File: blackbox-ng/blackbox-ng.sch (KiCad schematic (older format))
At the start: 5 parts

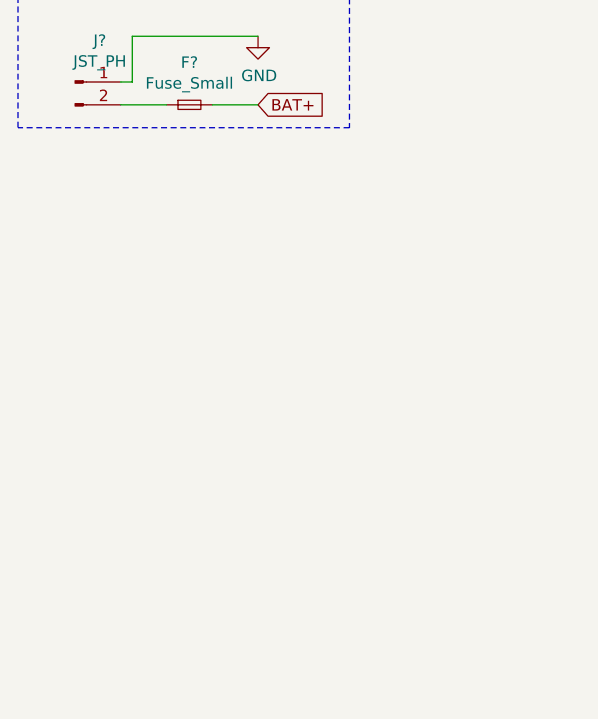
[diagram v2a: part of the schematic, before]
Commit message: add power led
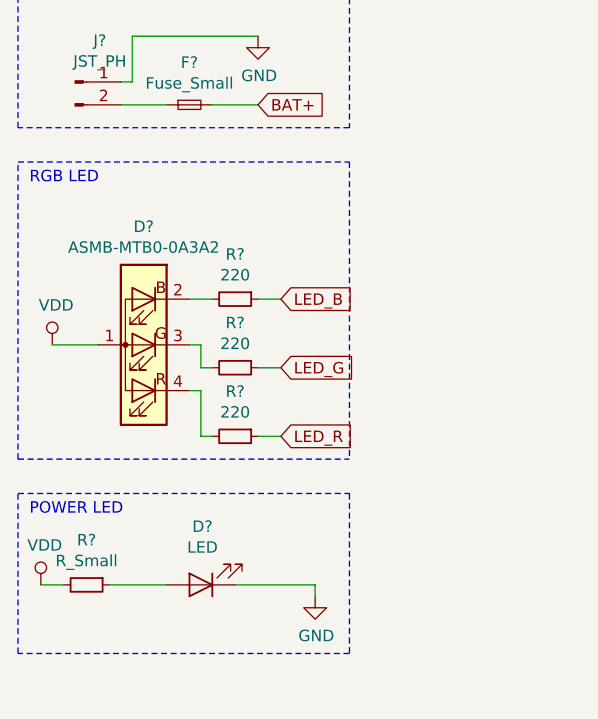
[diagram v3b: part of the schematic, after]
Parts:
- added D?: ASMB-MTB0-0A3A2, LED_SMD:LED_Avago_PLCC4_3.2x2.8mm_CW, symbol LED:ASMB-MTB0-0A3A2
- added D?: LED, symbol Device:LED
- added R? (x3): 220, symbol Device:R_Small
- added R?: R_Small, symbol Device:R_Small
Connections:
- net GND: now also D?.1 (K)
- net VDD: now also D?.1 (A), R?.2
- new net: D?.2 (BK), R?.2
- new net: D?.3 (GK), R?.2
- new net: D?.4 (RK), R?.2
- new net: D?.2 (A), R?.1
- new net LED_B: R?.1
- new net LED_G: R?.1
- new net LED_R: R?.1
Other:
- note added: "POWER LED"
- note added: "RGB LED"
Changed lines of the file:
@@
 Text Notes 650  1950 0    50   ~ 0
 BATTERY WITH FUSE
+$Comp
+L LED:ASMB-MTB0-0A3A2 D?
+U 1 1 5DF1D30C
+P 1150 3450
+F 0 "D?" H 1150 2933 50  0000 C CNN
+F 1 "ASMB-MTB0-0A3A2" H 1150 3024 50  0000 C CNN
+F 2 "LED_SMD:LED_Avago_PLCC4_3.2x2.8mm_CW" H 1150 3950 50  0001 C CNN
+F 3 "https://docs.broadcom.com/docs/AV02-4186EN" H 1150 3000 50  0001 C CNN
+	1    1150 3450
+	-1   0    0    1
+$EndComp
+$Comp
+L power:VDD #PWR?
+U 1 1 5DF22278
+P 750 3450
+F 0 "#PWR?" H 750 3300 50  0001 C CNN
+F 1 "VDD" H 767 3623 50  0000 C CNN
+F 2 "" H 750 3450 50  0001 C CNN
+F 3 "" H 750 3450 50  0001 C CNN
+	1    750  3450
+	1    0    0    -1
+$EndComp
+Wire Wire Line
+	750  3450 950  3450
+$Comp
+L Device:R_Small R?
+U 1 1 5DF22954
+P 1550 3250
+F 0 "R?" V 1354 3250 50  0000 C CNN
+F 1 "220" V 1445 3250 50  0000 C CNN
+F 2 "" H 1550 3250 50  0001 C CNN
+F 3 "~" H 1550 3250 50  0001 C CNN
+	1    1550 3250
+	0    1    1    0
+$EndComp
+$Comp
+L Device:R_Small R?
+U 1 1 5DF22E47
+P 1550 3550
+F 0 "R?" V 1354 3550 50  0000 C CNN
+F 1 "220" V 1445 3550 50  0000 C CNN
+F 2 "" H 1550 3550 50  0001 C CNN
+F 3 "~" H 1550 3550 50  0001 C CNN
+	1    1550 3550
+	0    1    1    0
+$EndComp
+$Comp
+L Device:R_Small R?
+U 1 1 5DF230BE
+P 1550 3850
+F 0 "R?" V 1354 3850 50  0000 C CNN
+F 1 "220" V 1445 3850 50  0000 C CNN
+F 2 "" H 1550 3850 50  0001 C CNN
+F 3 "~" H 1550 3850 50  0001 C CNN
+	1    1550 3850
+	0    1    1    0
+$EndComp
+Wire Wire Line
+	1350 3250 1450 3250
+Wire Wire Line
+	1350 3450 1400 3450
+Wire Wire Line
+	1400 3450 1400 3550
+Wire Wire Line
+	1400 3550 1450 3550
+Wire Wire Line
+	1350 3650 1400 3650
+Wire Wire Line
+	1400 3650 1400 3850
+Wire Wire Line
+	1400 3850 1450 3850
+Text GLabel 1750 3850 2    50   Input ~ 0
+LED_R
+Text GLabel 1750 3250 2    50   Input ~ 0
+LED_B
+Text GLabel 1750 3550 2    50   Input ~ 0
+LED_G
+Wire Wire Line
+	1650 3250 1750 3250
+Wire Wire Line
+	1650 3550 1750 3550
+Wire Wire Line
+	1750 3850 1650 3850
+Wire Notes Line
+	600  2650 2050 2650
+Wire Notes Line
+	2050 2650 2050 3950
+Wire Notes Line
+	600  3950 600  2650
+Wire Notes Line
+	600  3950 2050 3950
+Text Notes 650  2750 0    50   ~ 0
+RGB LED
+$Comp
+L Device:LED D?
+U 1 1 5DF2EFEC
+P 1400 4500
+F 0 "D?" H 1393 4245 50  0000 C CNN
+F 1 "LED" H 1393 4336 50  0000 C CNN
+F 2 "" H 1400 4500 50  0001 C CNN
+F 3 "~" H 1400 4500 50  0001 C CNN
+	1    1400 4500
+	-1   0    0    1
+$EndComp
+$Comp
+L power:GND #PWR?
+U 1 1 5DF30C94
+P 1900 4550
+F 0 "#PWR?" H 1900 4300 50  0001 C CNN
+F 1 "GND" H 1905 4377 50  0000 C CNN
+F 2 "" H 1900 4550 50  0001 C CNN
+F 3 "" H 1900 4550 50  0001 C CNN
+	1    1900 4550
+	1    0    0    -1
+$EndComp
+$Comp
+L Device:R_Small R?
+U 1 1 5DF31A81
+P 900 4500
+F 0 "R?" V 704 4500 50  0000 C CNN
+F 1 "R_Small" V 795 4500 50  0000 C CNN
+F 2 "" H 900 4500 50  0001 C CNN
+F 3 "~" H 900 4500 50  0001 C CNN
+	1    900  4500
+	0    1    1    0
+$EndComp
+$Comp
+L power:VDD #PWR?
+U 1 1 5DF32145
+P 700 4500
+F 0 "#PWR?" H 700 4350 50  0001 C CNN
+F 1 "VDD" H 717 4673 50  0000 C CNN
+F 2 "" H 700 4500 50  0001 C CNN
+F 3 "" H 700 4500 50  0001 C CNN
+	1    700  4500
+	1    0    0    -1
+$EndComp
+Wire Wire Line
+	1550 4500 1900 4500
+Wire Wire Line
+	1900 4500 1900 4550
+Wire Wire Line
+	1000 4500 1250 4500
+Wire Wire Line
+	700  4500 800  4500
+Text Notes 650  4200 0    50   ~ 0
+POWER LED
+Wire Notes Line
+	600  4100 2050 4100
+Wire Notes Line
+	2050 4100 2050 4800
+Wire Notes Line
+	2050 4800 600  4800
+Wire Notes Line
+	600  4800 600  4100
 $EndSCHEMATC

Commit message: add mpl
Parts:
- R?: value R_Small -> 1k
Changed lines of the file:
@@
 $Descr A4 11693 8268
 encoding utf-8
-Sheet 1 2
+Sheet 1 3
 Title ""
 Date ""
@@
 P 900 4500
 F 0 "R?" V 704 4500 50  0000 C CNN
-F 1 "R_Small" V 795 4500 50  0000 C CNN
+F 1 "1k" V 795 4500 50  0000 C CNN
 F 2 "" H 900 4500 50  0001 C CNN
 F 3 "~" H 900 4500 50  0001 C CNN
@@
 Wire Notes Line
 	600  4800 600  4100
+$Sheet
+S 900  5100 550  500
+U 5DF3873A
+F0 "MPL3115A2" 50
+F1 "MPL3115A2.sch" 50
+F2 "SCL" I R 1450 5400 50
+F3 "SDA" I R 1450 5300 50
+$EndSheet
 $EndSCHEMATC

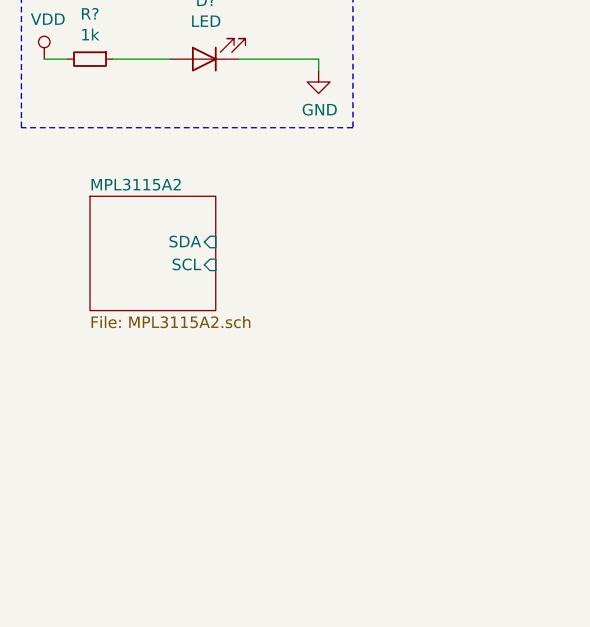
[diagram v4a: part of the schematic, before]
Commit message: add MPU9250 IMU
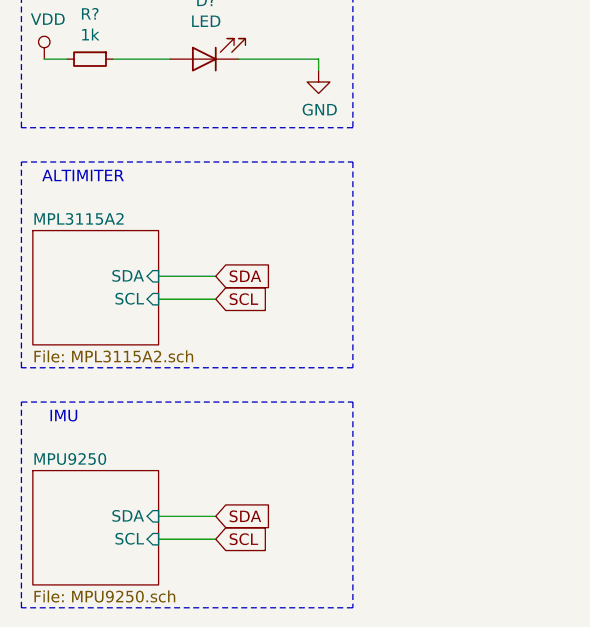
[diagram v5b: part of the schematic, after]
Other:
- note added: "ALTIMITER"
- note added: "IMU"
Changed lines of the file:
@@
 $Descr A4 11693 8268
 encoding utf-8
-Sheet 1 3
+Sheet 1 4
 Title ""
 Date ""
@@
 	600  4800 600  4100
 $Sheet
-S 900  5100 550  500
+S 650  5250 550  500
 U 5DF3873A
 F0 "MPL3115A2" 50
 F1 "MPL3115A2.sch" 50
-F2 "SCL" I R 1450 5400 50
-F3 "SDA" I R 1450 5300 50
+F2 "SCL" I R 1200 5550 50
+F3 "SDA" I R 1200 5450 50
 $EndSheet
+Wire Notes Line
+	600  4950 2050 4950
+Wire Notes Line
+	2050 4950 2050 5850
+Wire Notes Line
+	2050 5850 600  5850
+Wire Notes Line
+	600  5850 600  4950
+Text Notes 1050 5050 2    50   ~ 0
+ALTIMITER
+Text GLabel 1450 5450 2    50   Input ~ 0
+SDA
+Text GLabel 1450 5550 2    50   Input ~ 0
+SCL
+Wire Wire Line
+	1200 5550 1450 5550
+Wire Wire Line
+	1450 5450 1200 5450
+$Sheet
+S 650  6300 550  500
+U 5DF48A0D
+F0 "MPU9250" 50
+F1 "MPU9250.sch" 50
+F2 "SDA" I R 1200 6500 50
+F3 "SCL" I R 1200 6600 50
+$EndSheet
+Wire Notes Line
+	600  6000 2050 6000
+Wire Notes Line
+	2050 6000 2050 6900
+Wire Notes Line
+	2050 6900 600  6900
+Wire Notes Line
+	600  6900 600  6000
+Text Notes 850  6100 2    50   ~ 0
+IMU
+Text GLabel 1450 6500 2    50   Input ~ 0
+SDA
+Text GLabel 1450 6600 2    50   Input ~ 0
+SCL
+Wire Wire Line
+	1200 6500 1450 6500
+Wire Wire Line
+	1450 6600 1200 6600
 $EndSCHEMATC

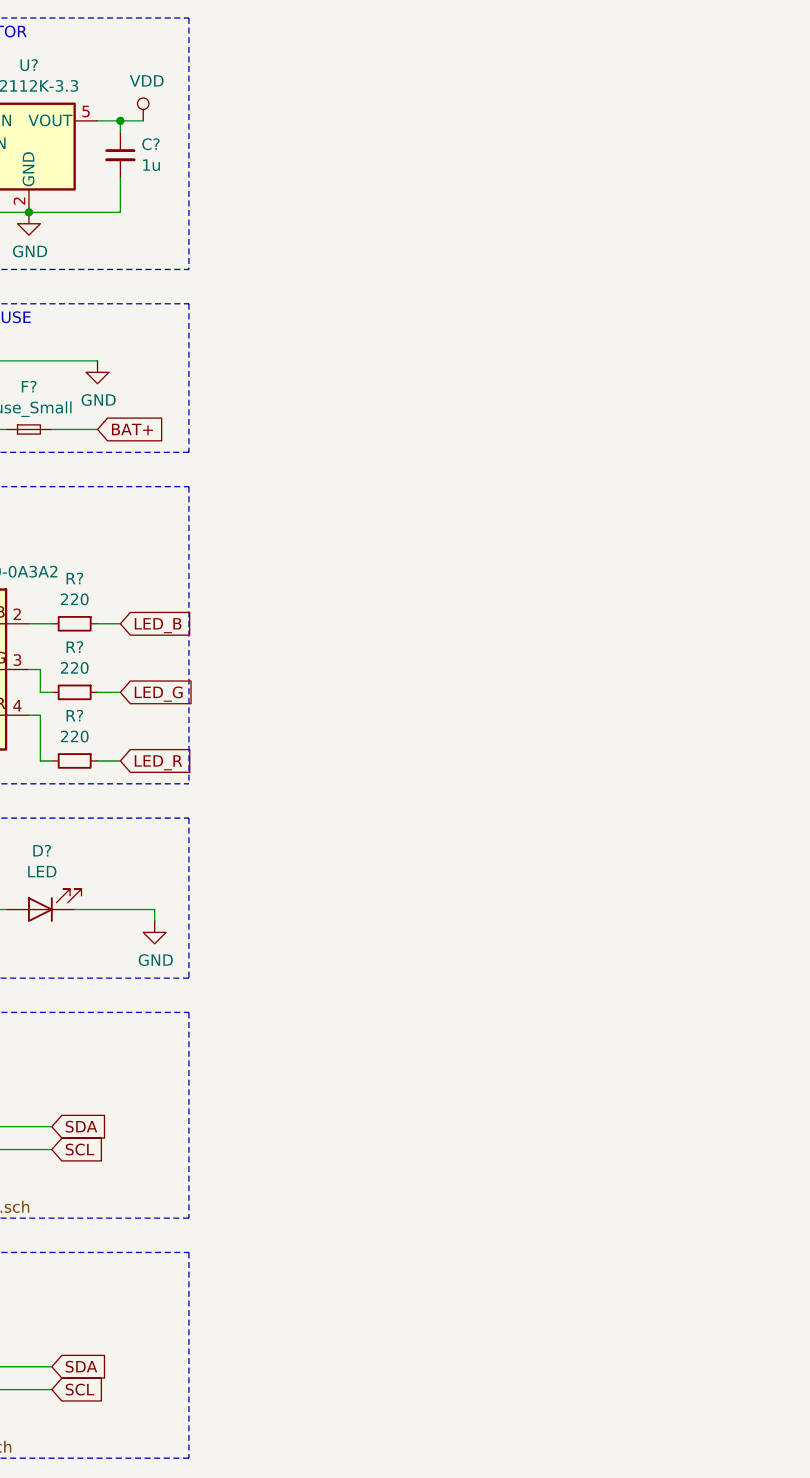
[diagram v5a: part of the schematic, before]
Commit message: add sdcard and buttons
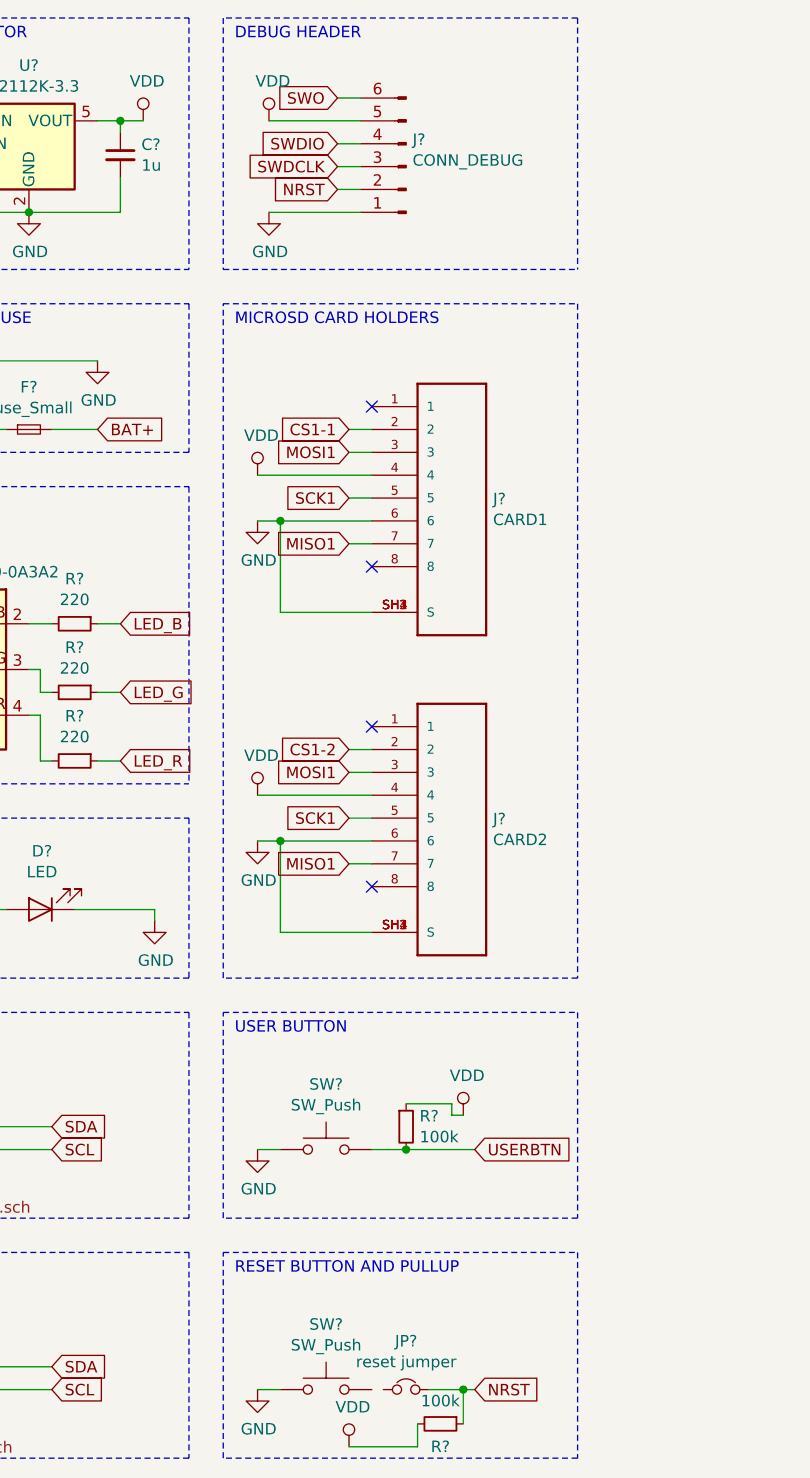
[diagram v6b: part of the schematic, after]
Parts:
- added J?: CONN_DEBUG, symbol Connector:Conn_01x06_Male
- added J?: CARD1, MOLEX_500901-0801, symbol bleh:500901-0801
- added J?: CARD2, MOLEX_500901-0801, symbol bleh:500901-0801
- added JP?: reset jumper, symbol Device:Jumper_NC_Small
- added R? (x2): 100k, symbol Device:R_Small
- added SW? (x2): SW_Push, symbol Switch:SW_Push
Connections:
- net GND: now also J?.1 (Pin_1), J?.6, J?.6, J?.SH1 (S), J?.SH1 (S), J?.SH2 (S), J?.SH2 (S), J?.SH3 (S), J?.SH3 (S), J?.SH4 (S), J?.SH4 (S), SW?.1, SW?.1
- net VDD: now also J?.4, J?.4, J?.5 (Pin_5), R?.1, R?.2
- new net CS1-1: J?.2
- new net CS1-2: J?.2
- new net MISO1: J?.7, J?.7
- new net MOSI1: J?.3, J?.3
- new net NRST: J?.2 (Pin_2), JP?.2, R?.1
- new net SCK1: J?.5, J?.5
- new net SWDCLK: J?.3 (Pin_3)
- new net SWDIO: J?.4 (Pin_4)
- new net SWO: J?.6 (Pin_6)
- new net USERBTN: R?.2, SW?.2
- no-connect marks 0 -> 4
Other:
- note added: "DEBUG HEADER"
- note added: "MICROSD CARD HOLDERS"
- note added: "RESET BUTTON AND PULLUP"
- note added: "USER BUTTON"
